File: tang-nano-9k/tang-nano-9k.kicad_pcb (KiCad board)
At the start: 2 copper layers, 39 parts, among them J1 UART_header, J2 Mini-DIN-6, J3 Trackball_breakout, J4 BBQ10KBD_PMOD, U1 Tang_Nano_9k_board, U10 GTL2002, U2 W5500_Breakout, U3 Audio_DAC_Breakout_UDA1334A, U4 GTL2002, U5 I2C_OLED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

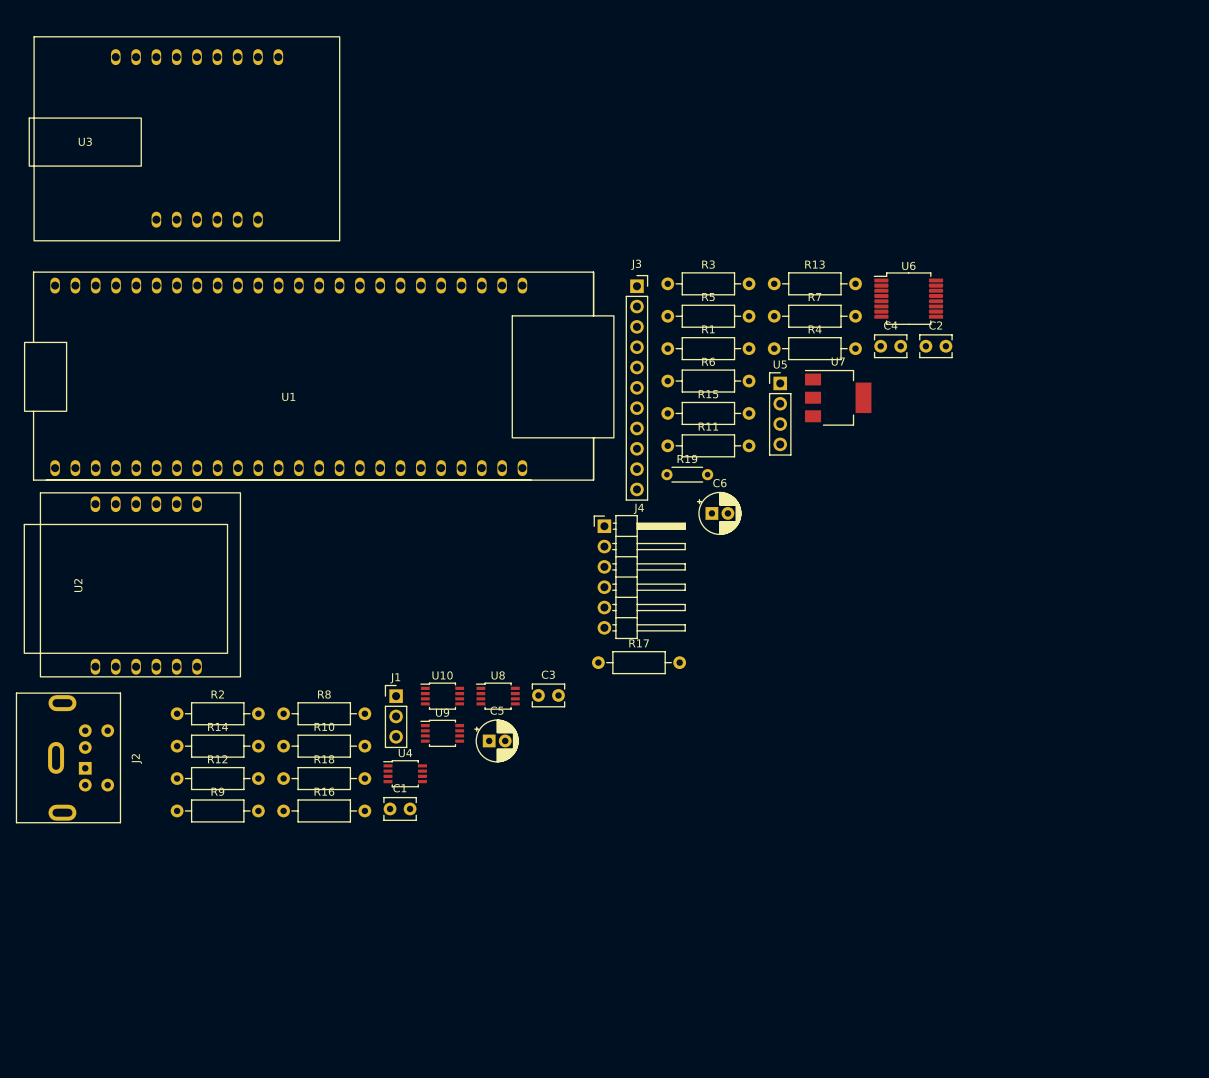
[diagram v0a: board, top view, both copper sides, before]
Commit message: Added pullups to GPIO expander INTn pin Initial placement and partial routing
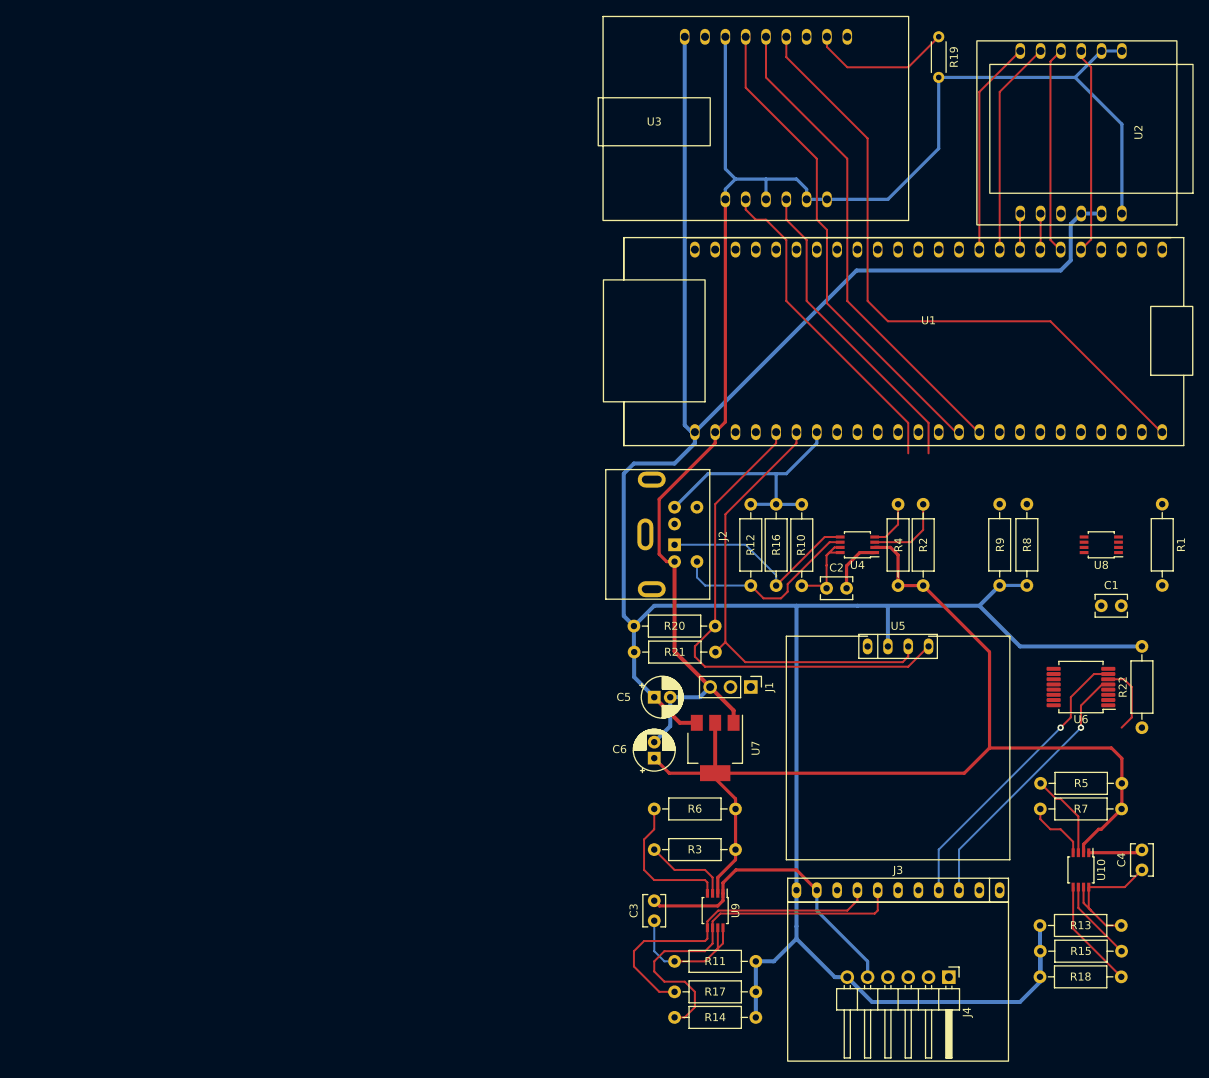
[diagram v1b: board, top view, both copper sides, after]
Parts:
- added R20: 4k7, Resistor_THT:R_Axial_DIN0207_L6.3mm_D2.5mm_P10.16mm_Horizontal, F.Cu at (152.4, 101.6)
- added R21: 4k7, Resistor_THT:R_Axial_DIN0207_L6.3mm_D2.5mm_P10.16mm_Horizontal, F.Cu at (152.4, 104.9)
- added R22: 4k7, Resistor_THT:R_Axial_DIN0207_L6.3mm_D2.5mm_P10.16mm_Horizontal, F.Cu at (215.9, 114.3)
- J3: footprint Connector_PinSocket_2.54mm:PinSocket_1x11_P2.54mm_Vertical -> Custom Library:Trackball_breakout
- U5: footprint Connector_PinHeader_2.54mm:PinHeader_1x04_P2.54mm_Vertical -> Custom Library:i2c_oled_128x64
- moved U2 128.7 mm to (207.0, 39.9), turned to 180 degrees
- moved R9 106.6 mm to (198.1, 96.5), turned to 90 degrees
- moved R18 97.7 mm to (203.2, 145.4)
- moved R2 96.9 mm to (188.6, 86.4), turned to -90 degrees
- moved R8 94.3 mm to (201.5, 96.5), turned to 90 degrees
- moved C1 92.5 mm to (210.8, 99.1)
- moved R13 86.8 mm to (203.2, 139.0)
- moved U10 82.7 mm to (208.3, 132.1), turned to -90 degrees
- moved R15 81.8 mm to (203.2, 142.2)
- moved U1 80.1 mm to (189.2, 65.9), turned to 180 degrees
- moved J3 79.9 mm to (185.4, 132.1), turned to 180 degrees
- moved R14 79.9 mm to (167.6, 150.5), turned to 180 degrees
- moved R12 79.5 mm to (167.0, 86.4), turned to -90 degrees
- moved J2 78.8 mm to (157.5, 91.4)
- moved U8 77.7 mm to (210.8, 91.4), turned to 180 degrees
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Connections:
- U1 pad 10: /ETH_RST -> /ETH_INT
- U1 pad 5: /ETH_INT -> /ETH_MOSI
- U1 pad 6: /ETH_MISO -> /ETH_SCK
- U1 pad 7: /ETH_MOSI -> /ETH_RST
- U1 pad 8: /ETH_SCK -> /ETH_MISO
- U6 pad 3: +3V3 -> Net-(U6-Pad3)
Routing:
- net +3V3: track 0.00 -> 341.7 mm
- net GND: track 0.00 -> 244.2 mm
- net +1V8: track 0.00 -> 132.4 mm
- net /I2S_BCLK: track 0.00 -> 80.9 mm
- net /SDA: track 0.00 -> 63.0 mm
- net /I2S_WSEL: track 0.00 -> 60.7 mm
- net /I2S_DATA: track 0.00 -> 60.5 mm
- net /SCL: track 0.00 -> 57.1 mm
- net /TRACKBALL_LFT_3V3: track 0.00 -> 47.1 mm
- net /TRACKBALL_RHT_3V3: track 0.00 -> 41.4 mm
- net /AUDIO_SF1: track 0.00 -> 40.9 mm
- net /AUDIO_SF0: track 0.00 -> 39.1 mm
- net /WHT: track 0.00 -> 36.9 mm, vias 0 -> 1
- net /GRN: track 0.00 -> 33.9 mm, vias 0 -> 1
- net +5V: track 0.00 -> 32.7 mm
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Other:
- rule pad_to_mask_clearance: 0 -> 0.05
